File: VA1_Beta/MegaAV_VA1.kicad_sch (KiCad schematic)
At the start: 176 parts, among them CN1 MD-90SM_MD2, P1 SMD_Conn_01x01, U1 4070, U2 74HCT123, U3 TS924, U4 THS7374, U5 ICS501, U6 TS922, U7 TS924, U8 AD723

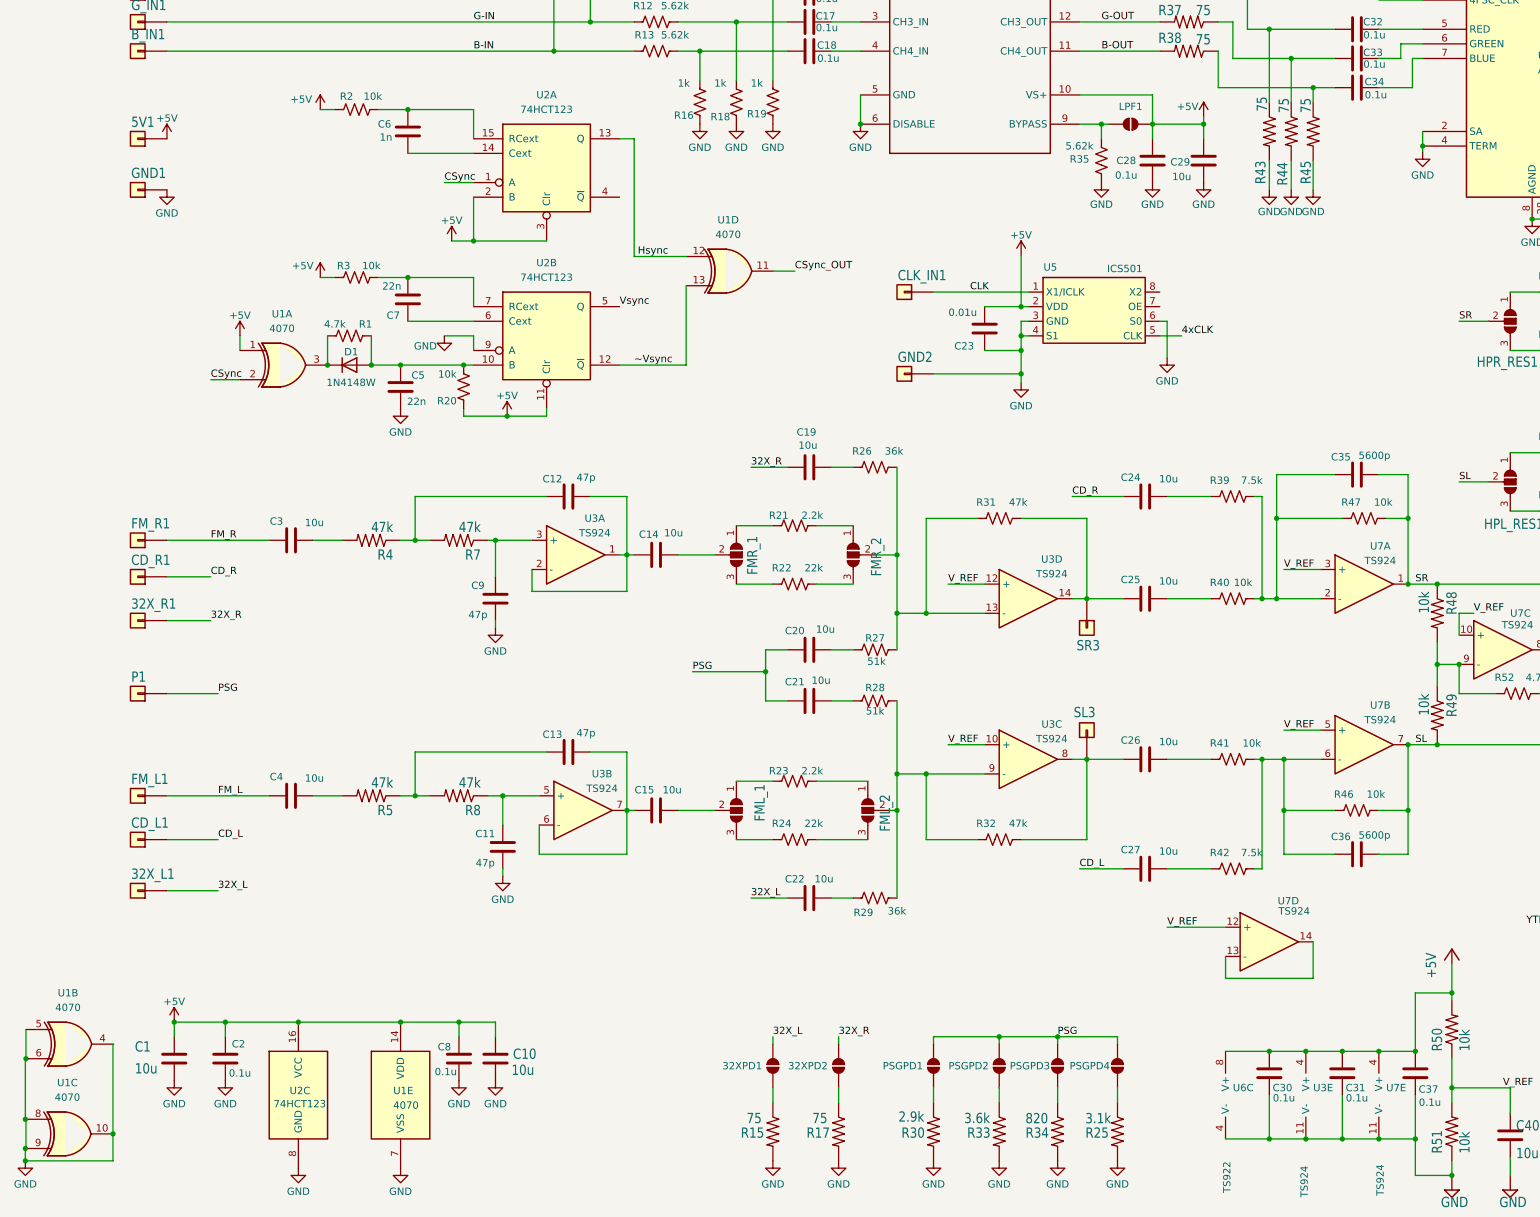
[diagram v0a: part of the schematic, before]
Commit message: Silkscreen fix
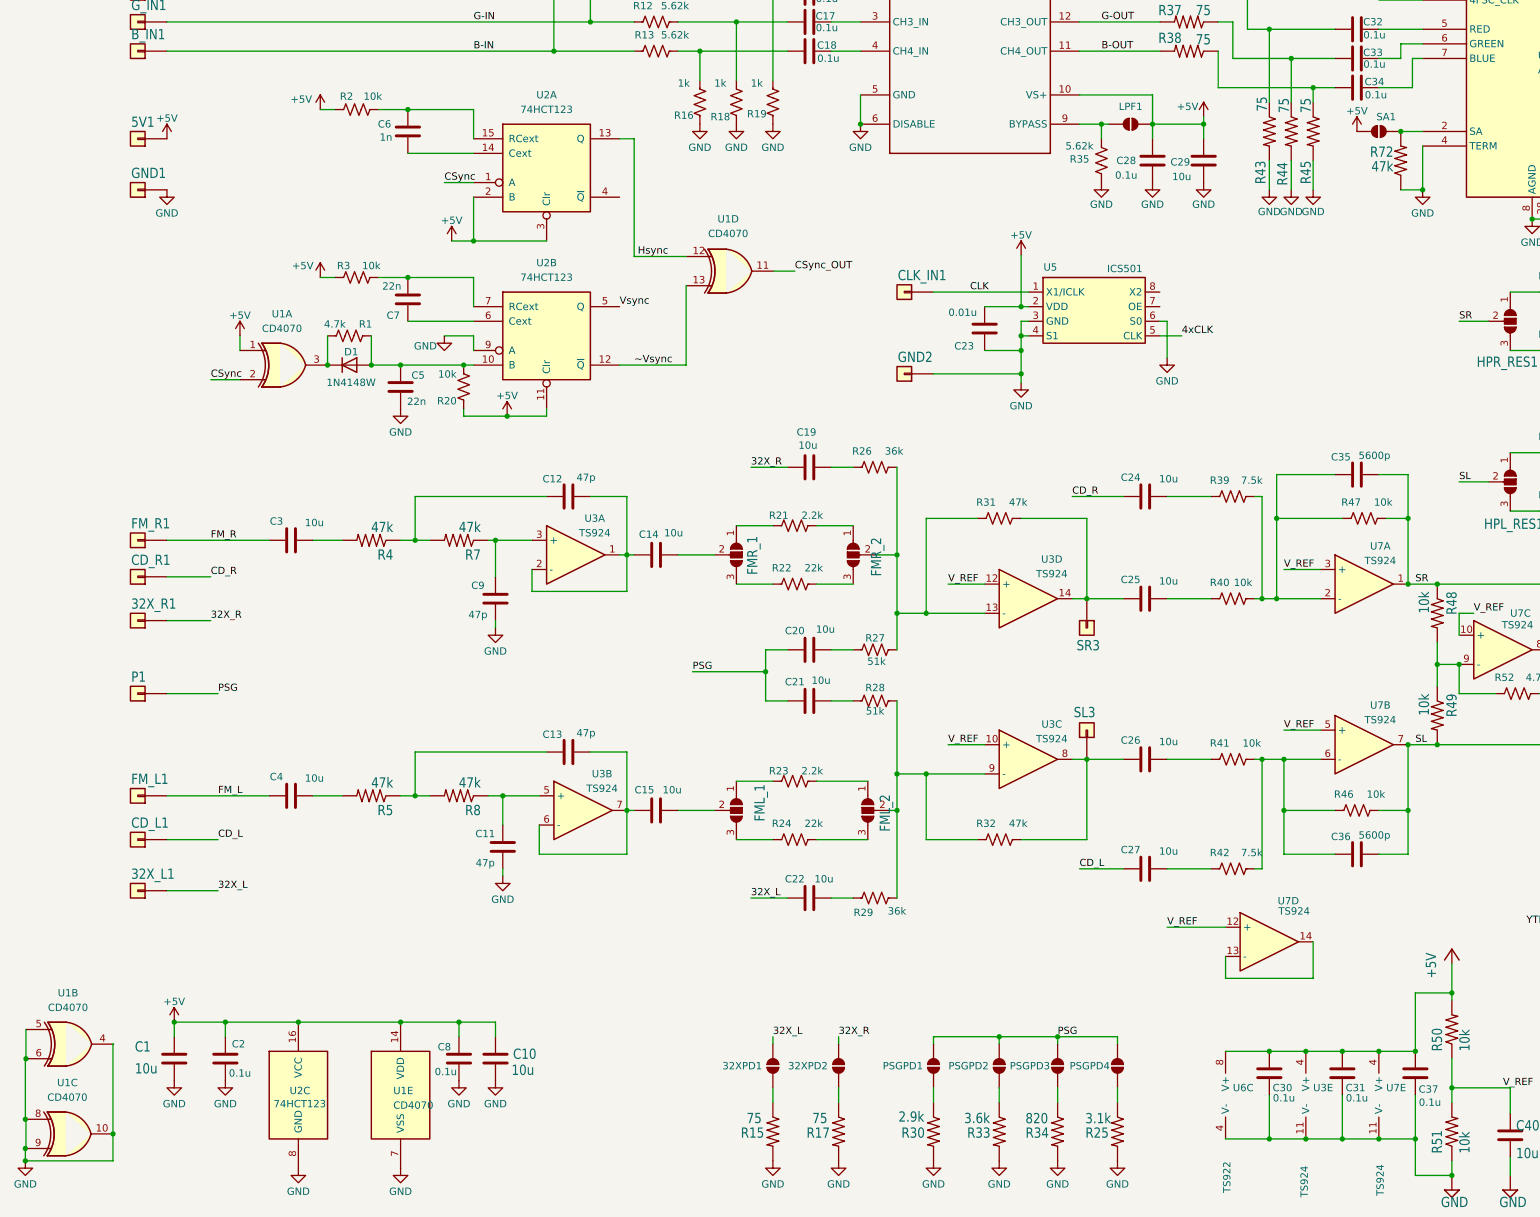
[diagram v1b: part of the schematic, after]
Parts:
- added R72: 47k, Resistor_SMD:R_0402_1005Metric, symbol 3bpV2A_RevC-eagle-import:R-US_R0603
- added SA1: ~, Jumper:SolderJumper-2_P1.3mm_Open_RoundedPad1.0x1.5mm, symbol Jumper:SolderJumper_2_Open
- U1: value 4070 -> CD4070
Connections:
- net +5V: now also SA1.1 (A)
- net GND: now also R72.1; no longer U8.2 (SA)
- new net: R72.2, SA1.2 (B), U8.2 (SA)
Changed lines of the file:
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@@
 	)
 	(junction
+		(at 265.43 85.09)
+		(diameter 0)
+		(color 0 0 0 0)
+	)
+	(junction
 		(at 69.85 229.87)
 		(diameter 0)
@@
 	)
 	(junction
-		(at 265.43 77.47)
-		(diameter 0)
-		(color 0 0 0 0)
-	)
-	(junction
 		(at 251.46 250.19)
 		(diameter 0)
@@
 	)
 	(junction
+		(at 261.62 74.93)
+		(diameter 0)
+		(color 0 0 0 0)
+	)
+	(junction
 		(at 48.26 229.87)
 		(diameter 0)
@@
 	(wire
 		(pts
-			(xy 265.43 74.93) (xy 265.43 77.47)
-		)
-		(stroke
-			(width 0)
-			(type default)
-		)
-	)
-	(wire
-		(pts
 			(xy 182.88 181.61) (xy 189.23 181.61)
 		)
@@
 	(wire
 		(pts
+			(xy 265.43 77.47) (xy 265.43 85.09)
+		)
+		(stroke
+			(width 0)
+			(type default)
+		)
+	)
+	(wire
+		(pts
 			(xy 167.64 68.58) (xy 167.64 73.66)
 		)
@@
 	(wire
 		(pts
+			(xy 265.43 85.09) (xy 261.62 85.09)
+		)
+		(stroke
+			(width 0)
+			(type default)
+		)
+	)
+	(wire
+		(pts
 			(xy 204.47 156.21) (xy 207.01 156.21)
 		)
@@
 	(wire
 		(pts
+			(xy 261.62 74.93) (xy 265.43 74.93)
+		)
+		(stroke
+			(width 0)
+			(type default)
+		)
+	)
+	(wire
+		(pts
 			(xy 306.07 102.87) (xy 312.42 102.87)
 		)
@@
 	(wire
 		(pts
-			(xy 265.43 77.47) (xy 265.43 78.486)
-		)
-		(stroke
-			(width 0)
-			(type default)
-		)
-	)
-	(wire
-		(pts
 			(xy 104.14 35.56) (xy 105.41 35.56)
 		)
@@
 			)
 		)
-		(property "Value" "4070"
+		(property "Value" "CD4070"
 			(at 86.36 244.348 0)
 			(effects
@@
 	)
 	(symbol
+		(lib_id "3bpV2A_RevC-eagle-import:R-US_R0603")
+		(at 261.62 80.01 90)
+		(unit 1)
+		(exclude_from_sim no)
+		(in_bom yes)
+		(on_board yes)
+		(dnp no)
+		(property "Reference" "R72"
+			(at 260.35 77.47 90)
+			(effects
+				(font
+					(size 1.778 1.5113)
+				)
+				(justify left bottom)
+			)
+		)
+		(property "Value" "47k"
+			(at 260.35 80.01 90)
+			(effects
+				(font
+					(size 1.778 1.5113)
+				)
+				(justify left bottom)
+			)
+		)
+		(property "Footprint" "Resistor_SMD:R_0402_1005Metric"
+			(at 261.62 80.01 0)
+			(effects
+				(font
+					(size 1.27 1.27)
+				)
+				(hide yes)
+			)
+		)
+		(property "Datasheet" ""
+			(at 261.62 80.01 0)
+			(effects
+				(font
+					(size 1.27 1.27)
+				)
+				(hide yes)
+			)
+		)
+		(property "Description" ""
+			(at 261.62 80.01 0)
+			(effects
+				(font
+					(size 1.27 1.27)
+				)
+				(hide yes)
+			)
+		)
+		(pin "1"
+		)
+		(pin "2"
+		)
+		(instances
+			(project "MegaAV_VA1"
+				(path "/672e6c7a-d310-45d1-a117-69a32c775d0f"
+					(reference "R72")
+					(unit 1)
+				)
+			)
+		)
+	)
+	(symbol
 		(lib_id "Jumper:SolderJumper_2_Open")
 		(at 180.34 237.49 90)
@@
 			)
 		)
-		(property "Value" "4070"
+		(property "Value" "CD4070"
 			(at 29.7769 227.3459 0)
 			(effects
@@
 	(symbol
 		(lib_id "Jumper:SolderJumper_2_Open")
+		(at 257.81 74.93 0)
+		(unit 1)
+		(exclude_from_sim no)
+		(in_bom yes)
+		(on_board yes)
+		(dnp no)
+		(property "Reference" "SA1"
+			(at 259.08 72.39 0)
+			(effects
+				(font
+					(size 1.27 1.27)
+				)
+			)
+		)
+		(property "Value" "~"
+			(at 257.81 71.12 0)
+			(effects
+				(font
+					(size 1.27 1.27)
+				)
+			)
+		)
+		(property "Footprint" "Jumper:SolderJumper-2_P1.3mm_Open_RoundedPad1.0x1.5mm"
+			(at 257.81 74.93 0)
+			(effects
+				(font
+					(size 1.27 1.27)
+				)
+				(hide yes)
+			)
+		)
+		(property "Datasheet" "~"
+			(at 257.81 74.93 0)
+			(effects
+				(font
+					(size 1.27 1.27)
+				)
+				(hide yes)
+			)
+		)
+		(property "Description" "Solder Jumper, 2-pole, open"
+			(at 257.81 74.93 0)
+			(effects
+				(font
+					(size 1.27 1.27)
+				)
+				(hide yes)
+			)
+		)
+		(pin "2"
+		)
+		(pin "1"
+		)
+		(instances
+			(project "MegaAV_VA1"
+				(path "/672e6c7a-d310-45d1-a117-69a32c775d0f"
+					(reference "SA1")
+					(unit 1)
+				)
+			)
+		)
+	)
+	(symbol
+		(lib_id "Jumper:SolderJumper_2_Open")
 		(at 109.22 35.56 180)
 		(unit 1)
@@
 	)
 	(symbol
+		(lib_id "power:+5V")
+		(at 254 74.93 0)
+		(unit 1)
+		(exclude_from_sim no)
+		(in_bom yes)
+		(on_board yes)
+		(dnp no)
+		(property "Reference" "#PWR054"
+			(at 254 78.74 0)
+			(effects
+				(font
+					(size 1.27 1.27)
+				)
+				(hide yes)
+			)
+		)
+		(property "Value" "+5V"
+			(at 254 71.374 0)
+			(effects
+				(font
+					(size 1.27 1.27)
+				)
+			)
+		)
+		(property "Footprint" ""
+			(at 254 74.93 0)
+			(effects
+				(font
+					(size 1.27 1.27)
+				)
+				(hide yes)
+			)
+		)
+		(property "Datasheet" ""
+			(at 254 74.93 0)
+			(effects
+				(font
+					(size 1.27 1.27)
+				)
+				(hide yes)
+			)
+		)
+		(property "Description" "Power symbol creates a global label with name \"+5V\""
+			(at 254 74.93 0)
+			(effects
+				(font
+					(size 1.27 1.27)
+				)
+				(hide yes)
+			)
+		)
+		(pin "1"
+		)
+		(instances
+			(project "MegaAV_VA1"
+				(path "/672e6c7a-d310-45d1-a117-69a32c775d0f"
+					(reference "#PWR054")
+					(unit 1)
+				)
+			)
+		)
+	)
+	(symbol
 		(lib_id "My_Library:SMD_Conn_01x01")
 		(at 41.91 207.01 0)
@@
 	(symbol
 		(lib_id "power:GND")
-		(at 265.43 78.486 0)
+		(at 265.43 85.09 0)
 		(unit 1)
 		(exclude_from_sim no)
@@
 		(dnp no)
 		(property "Reference" "#PWR053"
-			(at 265.43 84.836 0)
+			(at 265.43 91.44 0)
 			(effects
 				(font
@@
 		)
 		(property "Value" "GND"
-			(at 265.43 82.55 0)
+			(at 265.43 89.154 0)
 			(effects
 				(font
@@
 		)
 		(property "Footprint" ""
-			(at 265.43 78.486 0)
+			(at 265.43 85.09 0)
 			(effects
 				(font
@@
 		)
 		(property "Datasheet" ""
-			(at 265.43 78.486 0)
+			(at 265.43 85.09 0)
 			(effects
 				(font
@@
 		)
 		(property "Description" "Power symbol creates a global label with name \"GND\" , ground"
-			(at 265.43 78.486 0)
+			(at 265.43 85.09 0)
 			(effects
 				(font
@@
 			)
 		)
-		(property "Value" "4070"
+		(property "Value" "CD4070"
 			(at 67.0052 109.22 0)
 			(effects
@@
 		(fields_autoplaced yes)
 		(property "Reference" "U1"
-			(at 144.6216 90.334 0)
+			(at 144.6216 90.17 0)
 			(effects
 				(font
@@
 			)
 		)
-		(property "Value" "4070"
-			(at 144.6216 92.874 0)
+		(property "Value" "CD4070"
+			(at 144.6216 92.71 0)
 			(effects
 				(font
@@
 			)
 		)
-		(property "Value" "4070"
+		(property "Value" "CD4070"
 			(at 29.6738 242.9624 0)
 			(effects
